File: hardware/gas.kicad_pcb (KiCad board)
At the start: 2 copper layers, 65 x 30 mm, 25 parts, among them P1 CON-SENSOR2, P2 BOOT, P3 DEBUG, P4 Gas Sensor, U1 XMC1404, U2 DRILL, U3 DRILL, U4 DRILL, U5 DRILL, X1 16MHz

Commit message: pcb design
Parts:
- added G***: LOGO, kicad-libraries:Logo_CoMCU, B.Cu at (158.5, 112.5)
- added G***: LOGO, kicad-libraries:Logo_31x31, F.Cu at (161.5, 99.7)
- added VAL: WEEE_7mm, kicad-libraries:WEEE_7mm, B.Cu at (150.0, 112.5)
- added VAL: CE_5mm, kicad-libraries:CE_5mm, B.Cu at (142.5, 112.5)
- moved C10 8.66 mm to (181.2, 106.3), turned to 270 degrees
- moved C11 8.41 mm to (179.5, 105.8), turned to 90 degrees
- moved D3 7.34 mm to (150.0, 124.5)
- moved P3 0.80 mm to (144.3, 100.0), turned to 180 degrees
- moved C1 0.70 mm to (124.4, 110.0)
- moved C2 0.60 mm to (126.0, 109.8)
- moved P2 0.07 mm to (146.8, 100.0)
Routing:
- net GND: track 30.5 -> 49.2 mm, vias 11 -> 17
- net Net-(P3-Pad1): track 0.00 -> 16.2 mm, vias 0 -> 2
- net VCC: track 122.9 -> 138.0 mm
- net Net-(P2-Pad2): track 0.00 -> 8.24 mm, vias 0 -> 2
- net Net-(D3-Pad2): track 3.23 -> 9.15 mm
- added copper zone on B.Cu, net GND
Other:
- board text added: "Status"
- board text added: "tinkerforge.com"

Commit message: final pcb design
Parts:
- added Fiducial_Mark: VAL**, kicad-libraries:Fiducial_Mark, F.Cu at (126.0, 86.0)
- added Fiducial_Mark: VAL**, kicad-libraries:Fiducial_Mark, F.Cu at (126.0, 104.0)
- added Fiducial_Mark: VAL**, kicad-libraries:Fiducial_Mark, F.Cu at (170.0, 87.0)
- added Fiducial_Mark: VAL**, kicad-libraries:Fiducial_Mark, F.Cu at (170.0, 103.0)
- moved C1 17.7 mm to (126.9, 92.5)
- moved C10 17.7 mm to (183.7, 88.8)
- moved C11 17.7 mm to (182.0, 88.3)
- moved C2 17.7 mm to (128.5, 92.3)
- moved C3 17.7 mm to (147.5, 102.3)
- moved C4 17.7 mm to (138.7, 94.2)
- moved C5 17.7 mm to (147.5, 100.6)
- moved C6 17.7 mm to (140.1, 94.2)
- moved C7 17.7 mm to (127.1, 99.9)
- moved C8 17.7 mm to (153.5, 97.8)
- moved C9 17.7 mm to (153.5, 92.2)
- moved D3 17.7 mm to (152.5, 107.0)
- moved G*** 17.7 mm to (161.0, 95.0)
- moved G*** 17.7 mm to (164.0, 82.2)
- moved P1 17.7 mm to (120.0, 95.0)
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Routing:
- net Net-(D3-Pad2): track 9.15 -> 1.79 mm
- net Net-(R1-Pad1): track 5.05 -> 10.2 mm, vias 0 -> 2
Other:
- net class Default: clearance 0.2 -> 0.149
- rule trace_clearance: 0.2 -> 0.149
- board text added: "Gas 1.0"

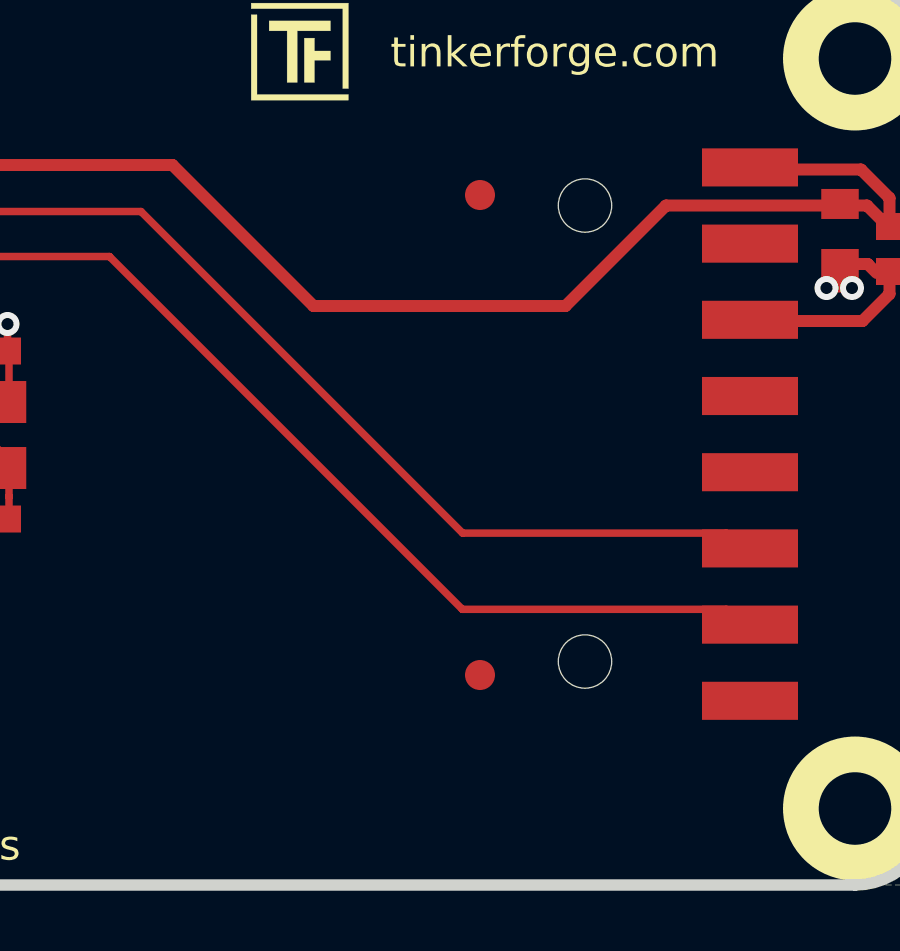
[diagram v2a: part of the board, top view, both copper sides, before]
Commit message: added fiducial marks
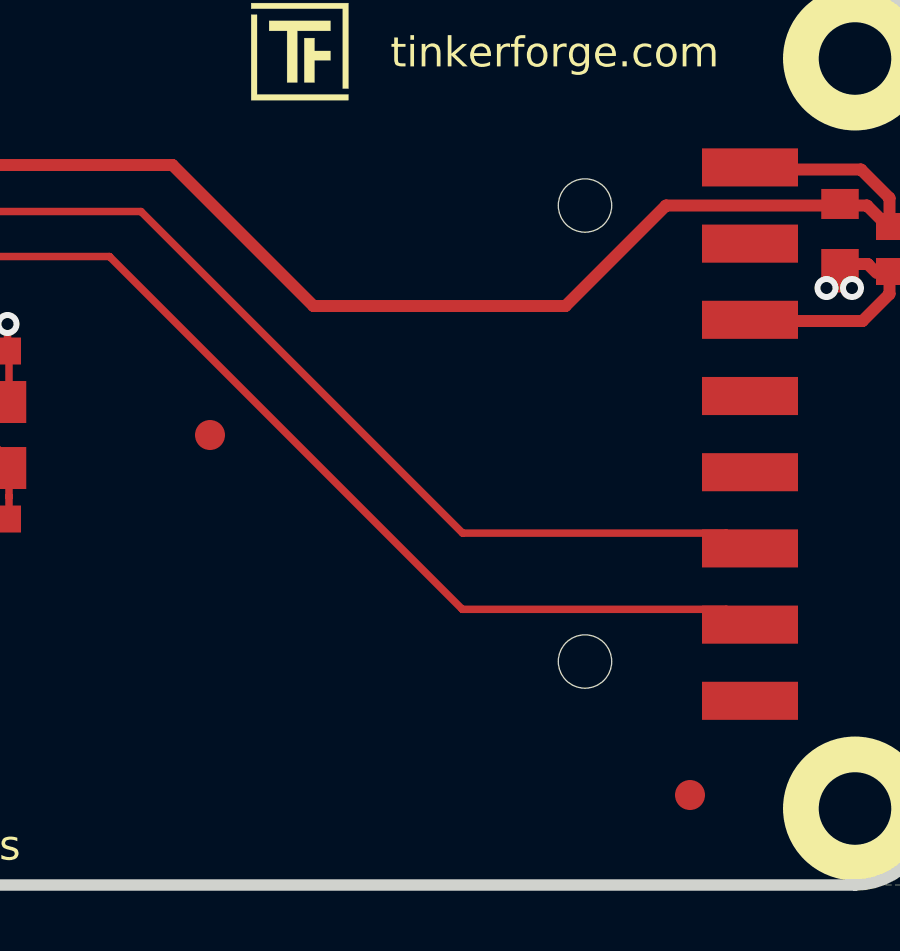
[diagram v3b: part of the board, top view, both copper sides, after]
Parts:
- moved Fiducial_Mark 12.0 mm to (161.0, 95.0)
- moved Fiducial_Mark 8.06 mm to (177.0, 107.0)
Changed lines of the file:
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@@
   )
   (module kicad-libraries:Fiducial_Mark (layer F.Cu)
-    (at 170 87)
+    (at 161 95)
     (attr smd)
     (fp_text reference Fiducial_Mark (at 0 0) (layer F.SilkS) hide
@@
   )
   (module kicad-libraries:Fiducial_Mark (layer F.Cu)
-    (at 170 103)
+    (at 177 107)
     (attr smd)
     (fp_text reference Fiducial_Mark (at 0 0) (layer F.SilkS) hide

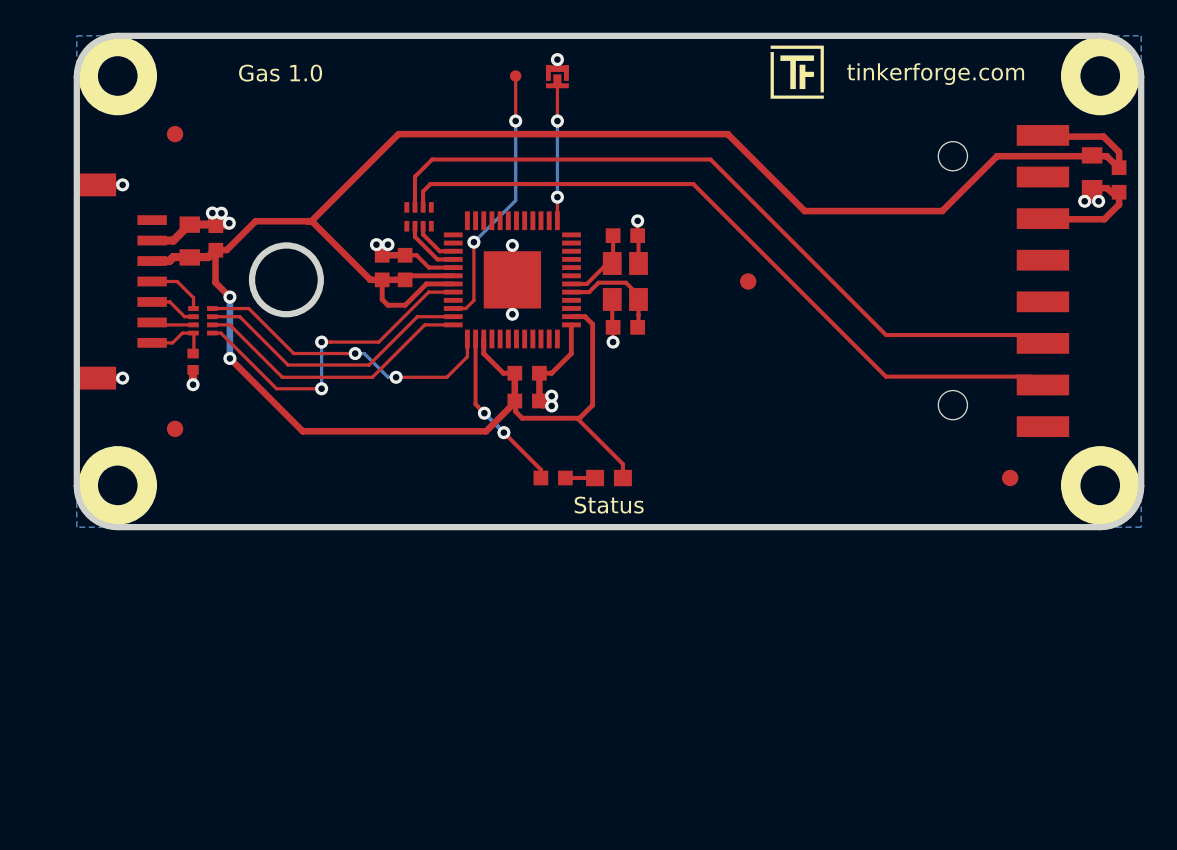
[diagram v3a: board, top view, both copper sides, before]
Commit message: changed mcu to xmc 1300, new pcb design,
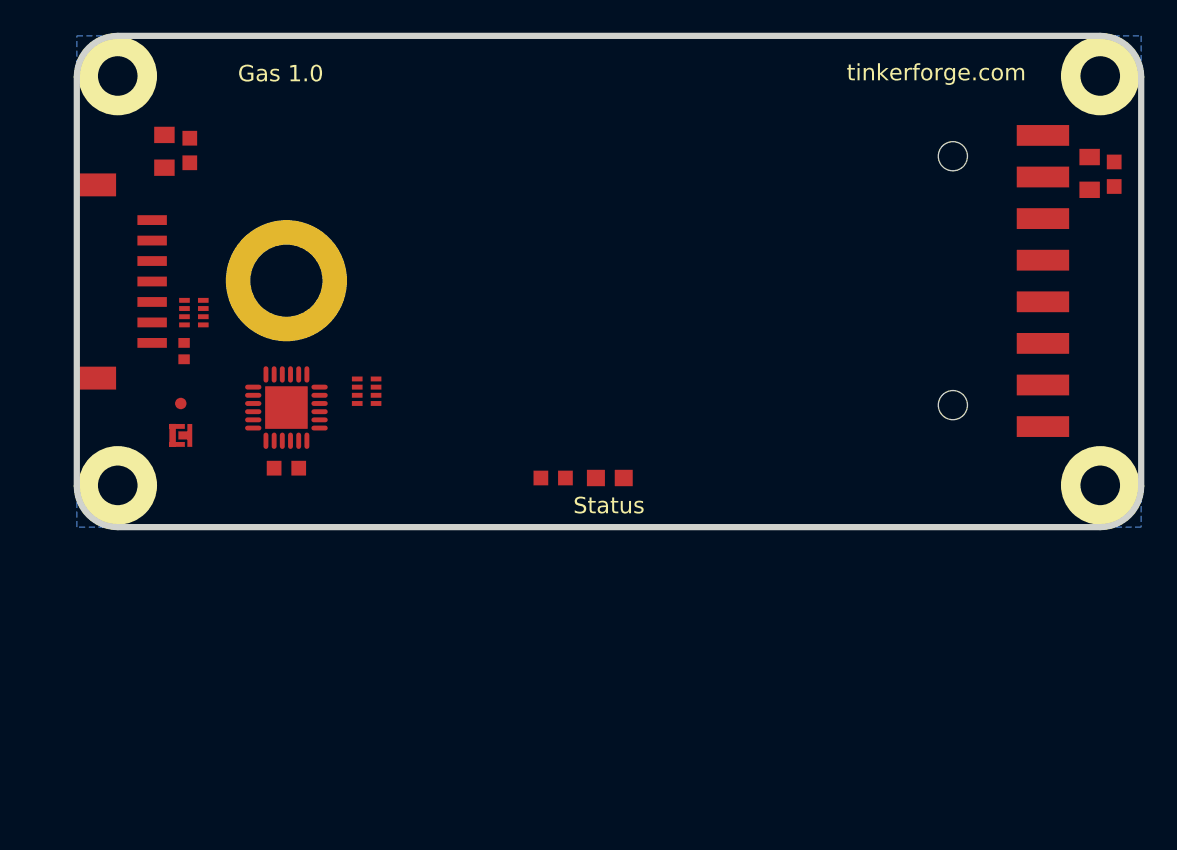
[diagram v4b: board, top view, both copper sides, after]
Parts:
- removed C10: 100n, kicad-libraries:C0603F
- removed C11: 10uF, kicad-libraries:C0805
- removed C7: 220pF, kicad-libraries:C0402F
- removed C8, C9: 10pF, kicad-libraries:C0603F
- removed D3: blue, kicad-libraries:D0603E
- removed Fiducial_Mark (x4): VAL**, kicad-libraries:Fiducial_Mark
- removed G***: LOGO, kicad-libraries:Logo_CoMCU
- removed G***: LOGO, kicad-libraries:Logo_31x31
- removed VAL: WEEE_7mm, kicad-libraries:WEEE_7mm
- removed VAL: CE_5mm, kicad-libraries:CE_5mm
- removed X1: 16MHz, kicad-libraries:CRYSTAL_3225
- added D1: blue, kicad-libraries:D0603E, F.Cu at (152.6, 107.0)
- added REF**: WA-SMSI-M3-SPACER, kicad-libraries:WA-SMSI-M3-SPACER, F.Cu at (132.8, 95.0)
- C1: value 10uF -> 220pF; footprint kicad-libraries:C0805 -> kicad-libraries:C0402F
- C2: value 1uF -> 10uF; footprint kicad-libraries:C0603F -> kicad-libraries:C0805
- C3: value 100nF -> 1uF
- C5: value 100nF -> 10uF; footprint kicad-libraries:C0603F -> kicad-libraries:C0805
- C6: value 220nF -> 100n
- P2: value BOOT -> DEBUG; footprint kicad-libraries:SolderJumper -> kicad-libraries:DEBUG_PAD
- P3: value DEBUG -> BOOT; footprint kicad-libraries:DEBUG_PAD -> kicad-libraries:SolderJumper
- U1: value XMC1404 -> XMC1300; footprint kicad-libraries:QFN48-EP2 -> kicad-libraries:QFN24-4x4mm-0.5mm
- moved C6 43.7 mm to (183.3, 88.5), turned to 270 degrees
- moved C5 36.5 mm to (181.8, 88.4), turned to 90 degrees
- moved P2 30.4 mm to (126.3, 102.5)
- moved P3 30.0 mm to (126.3, 104.4), turned to 0 degrees
- moved C3 25.7 mm to (126.9, 87.0), turned to 90 degrees
- moved U1 15.9 mm to (132.8, 102.7), turned to 0 degrees
- moved C4 13.6 mm to (132.8, 106.4), turned to 180 degrees
- moved RP2 11.1 mm to (137.7, 101.7), turned to 270 degrees
- moved C1 6.73 mm to (126.5, 99.2)
- moved C2 6.15 mm to (125.3, 87.0), turned to 90 degrees
- moved RP1 0.74 mm to (127.2, 96.9)
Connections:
- C1 pad 1: GND -> Net-(C1-Pad1)
- C1 pad 2: VCC -> GND
- C3 pad 1: VCC -> GND
- C3 pad 2: GND -> VCC
- C5 pad 1: VCC -> GND
- C5 pad 2: GND -> VCC
- P1 pad 1: (no net) -> +5V
- P1 pad 7: Net-(C7-Pad1) -> Net-(C1-Pad1)
- P2 pad 1: GND -> Net-(P2-Pad1)
- P3 pad 1: Net-(P3-Pad1) -> GND
- P4 pad 1: (no net) -> Net-(P4-Pad1)
- P4 pad 4: (no net) -> Net-(P4-Pad4)
- P4 pad 5: (no net) -> Net-(P4-Pad5)
- P4 pad 7: (no net) -> Net-(P4-Pad7)
- RP1 pad 4: Net-(C7-Pad1) -> Net-(C1-Pad1)
- RP2 pad 1: (no net) -> Net-(RP2-Pad1)
- RP2 pad 4: (no net) -> Net-(RP2-Pad4)
- RP2 pad 5: (no net) -> Net-(RP2-Pad5)
- RP2 pad 8: (no net) -> Net-(RP2-Pad8)
- U1 pad 1: Net-(P2-Pad2) -> S-MISO
- U1 pad 10: (no net) -> VCC
- U1 pad 11: (no net) -> Net-(U1-Pad11)
- U1 pad 12: (no net) -> Net-(U1-Pad12)
- U1 pad 13: (no net) -> Net-(U1-Pad13)
- U1 pad 14: (no net) -> Net-(R1-Pad1)
- U1 pad 15: GS_TX -> Net-(U1-Pad15)
- U1 pad 16: GS_RX -> Net-(U1-Pad16)
- U1 pad 17: GND -> GS_TX
- U1 pad 18: VCC -> GS_RX
- U1 pad 19: VCC -> Net-(U1-Pad19)
- U1 pad 2: (no net) -> Net-(U1-Pad2)
- U1 pad 20: S-MISO -> Net-(U1-Pad20)
- U1 pad 21: (no net) -> Net-(U1-Pad21)
- U1 pad 22: Net-(P3-Pad1) -> S-CS
- U1 pad 3: (no net) -> Net-(P2-Pad1)
- U1 pad 4: (no net) -> Net-(U1-Pad4)
- U1 pad 5: (no net) -> Net-(P3-Pad2)
- U1 pad 6: (no net) -> Net-(U1-Pad6)
- U1 pad 7: (no net) -> Net-(U1-Pad7)
- U1 pad 8: (no net) -> Net-(U1-Pad8)
- U1 pad 9: (no net) -> GND
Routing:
- net VCC: track 138.0 -> 0.00 mm, vias 2 -> 0
- net GND: track 49.2 -> 0.00 mm, vias 17 -> 0
- net Net-(P4-Pad3): track 45.1 -> 0.00 mm
- net Net-(P4-Pad2): track 43.9 -> 0.00 mm
- net S-MISO: track 20.2 -> 0.00 mm, vias 2 -> 0
- net S-CS: track 18.9 -> 0.00 mm, vias 2 -> 0
- net S-MOSI: track 17.4 -> 0.00 mm
- net S-CLK: track 17.2 -> 0.00 mm
- net Net-(P3-Pad1): track 16.2 -> 0.00 mm, vias 2 -> 0
- net Net-(R1-Pad1): track 10.2 -> 0.00 mm, vias 2 -> 0
- net Net-(P2-Pad2): track 8.64 -> 0.00 mm, vias 2 -> 0
- net Net-(C8-Pad1): track 6.65 -> 0.00 mm
- net Net-(C9-Pad1): track 4.86 -> 0.00 mm
- net Net-(C7-Pad1): track 4.07 -> 0.00 mm
- net GS_RX: track 3.63 -> 0.00 mm
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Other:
- outline, holes or cut-outs redrawn

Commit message: changed to xmc1300, new pcb design for part clearance, added smd M3 spacer
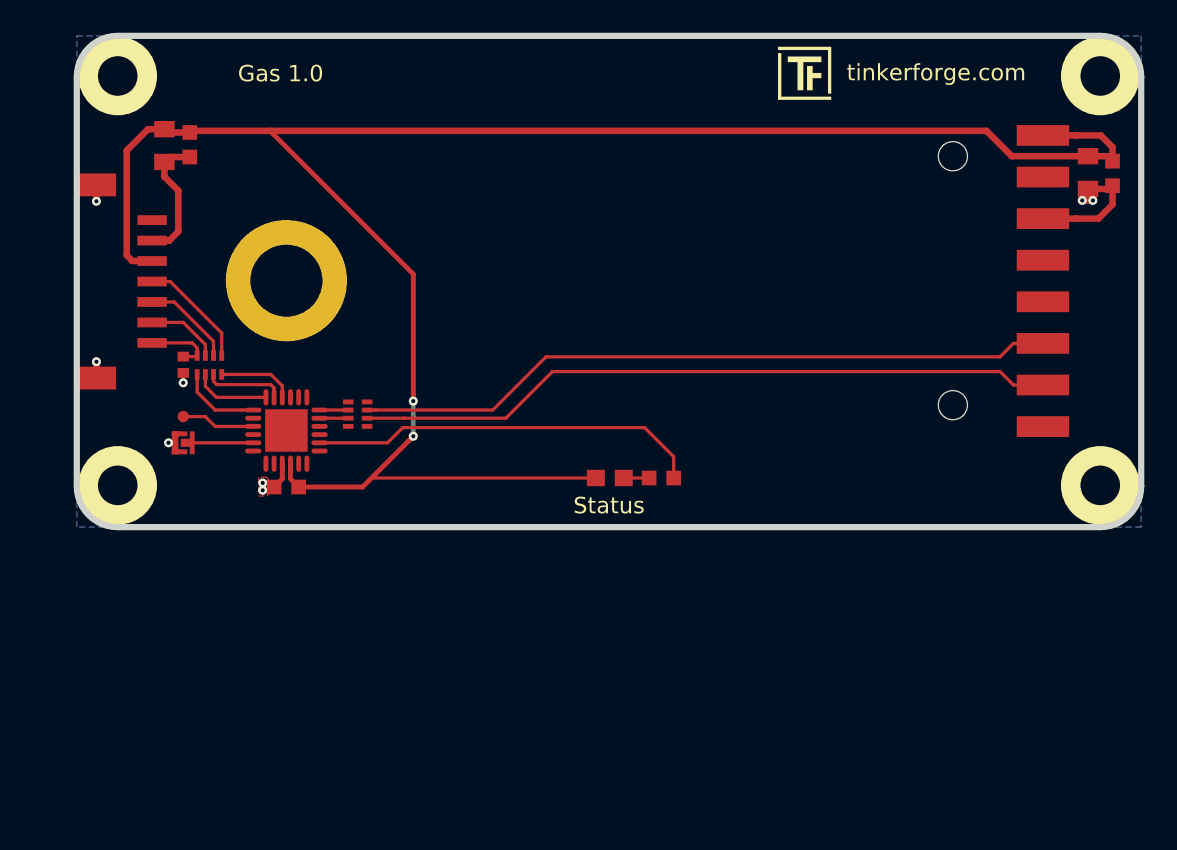
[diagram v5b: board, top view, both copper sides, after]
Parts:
- added G***: LOGO, kicad-libraries:Logo_31x31, F.Cu at (164.4, 82.3)
- added G***: LOGO, kicad-libraries:Logo_CoMCU, B.Cu at (159.0, 95.0)
- added VAL: WEEE_7mm, kicad-libraries:WEEE_7mm, B.Cu at (152.5, 95.0)
- added VAL: CE_5mm, kicad-libraries:CE_5mm, B.Cu at (146.5, 95.0)
- moved R1 6.61 mm to (155.7, 107.0), turned to 180 degrees
- moved RP1 3.34 mm to (128.1, 100.1), turned to 180 degrees
- moved RP2 1.50 mm to (137.2, 103.1)
- moved U1 1.40 mm to (132.8, 104.1)
- moved C4 1.15 mm to (132.8, 107.5)
- moved C1 0.84 mm to (126.5, 100.1)
- moved P2 0.81 mm to (126.5, 103.2)
- moved P3 0.47 mm to (126.5, 104.8)
- moved C2 0.35 mm to (125.3, 86.7)
- moved C3 0.35 mm to (126.9, 86.7)
- moved C5 0.11 mm to (181.8, 88.3)
- moved C6 0.11 mm to (183.2, 88.4)
- turned D1 to 0 degrees
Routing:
- net VCC: track 0.00 -> 121.8 mm, vias 0 -> 2
- net Net-(P4-Pad3): track 0.00 -> 43.0 mm
- net Net-(P4-Pad2): track 0.00 -> 42.8 mm
- net GND: track 0.00 -> 25.9 mm, vias 0 -> 8
- net Net-(R1-Pad1): track 0.00 -> 24.0 mm
- net Net-(P1-Pad4): track 0.00 -> 7.43 mm
- net Net-(P1-Pad5): track 0.00 -> 5.62 mm
- net S-MISO: track 0.00 -> 4.96 mm
- net S-CLK: track 0.00 -> 4.87 mm
- net Net-(C1-Pad1): track 0.00 -> 4.83 mm
- net S-MOSI: track 0.00 -> 4.70 mm
- net S-CS: track 0.00 -> 4.69 mm
- net Net-(P2-Pad1): track 0.00 -> 4.52 mm
- net Net-(P1-Pad6): track 0.00 -> 4.48 mm
- net Net-(P3-Pad2): track 0.00 -> 4.12 mm
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- added copper zone on F.Cu, net GND
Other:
- rule trace_min: 0.2 -> 0.1
- rule via_min_drill: 0.3 -> 0.25
